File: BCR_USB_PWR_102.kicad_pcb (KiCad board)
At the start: 2 copper layers, 21.8 x 13.2 mm, 2 parts, among them CN1 DB9_Female, CN2 UE27AC54100

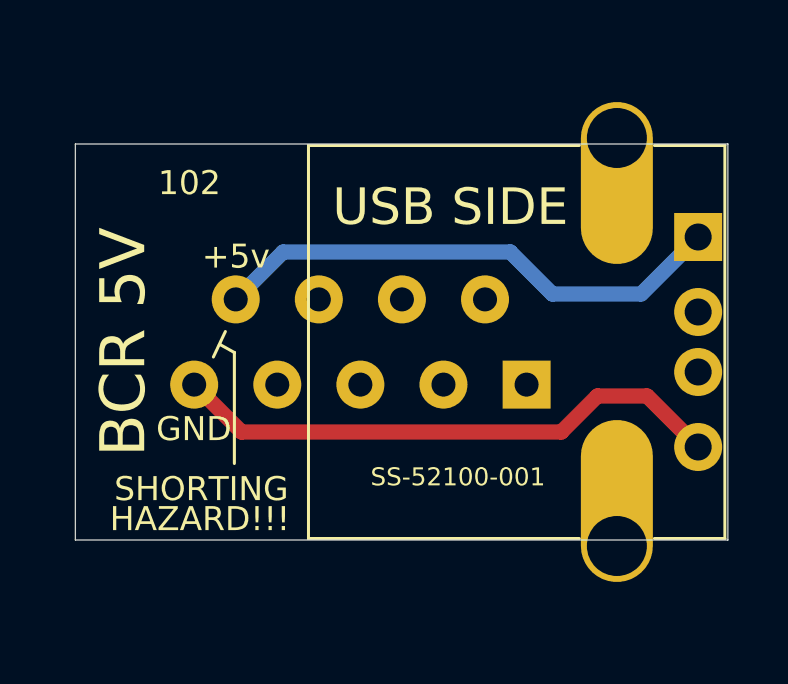
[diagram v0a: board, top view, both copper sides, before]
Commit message: rename NEC to up_long, and a short up version that covers up the shorting hazard
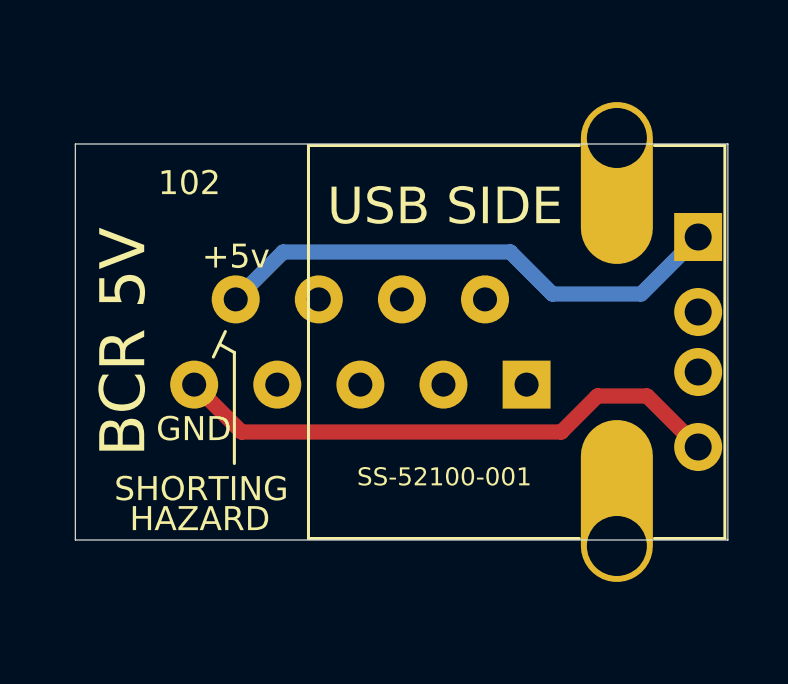
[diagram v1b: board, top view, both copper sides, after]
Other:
- board text added: "HAZARD"
- board text removed: "HAZARD!!!"
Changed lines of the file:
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@@
     (effects (font (size 0.8 0.8) (thickness 0.08)))
   )
-  (gr_text HAZARD!!! (at 121.65 101.658) (layer F.SilkS)
+  (gr_text HAZARD (at 121.65 101.658) (layer F.SilkS)
     (effects (font (size 0.8 0.8) (thickness 0.08)))
   )
@@
     (effects (font (size 0.6 0.6) (thickness 0.1)) (justify mirror))
   )
-  (gr_text SS-52100-001 (at 130.25 100.258) (layer F.SilkS)
+  (gr_text SS-52100-001 (at 129.8 100.258) (layer F.SilkS)
     (effects (font (size 0.6 0.6) (thickness 0.1)))
   )
@@
     (effects (font (size 1.2192 1.2192) (thickness 0.2032)) (justify mirror))
   )
-  (gr_text "USB SIDE" (at 130 91.258) (layer F.SilkS)
+  (gr_text "USB SIDE" (at 129.825 91.233) (layer F.SilkS)
     (effects (font (size 1.2192 1.2192) (thickness 0.2032)))
   )

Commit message: Add BCR_Breakout. Rename repo to BCR_Breakout.
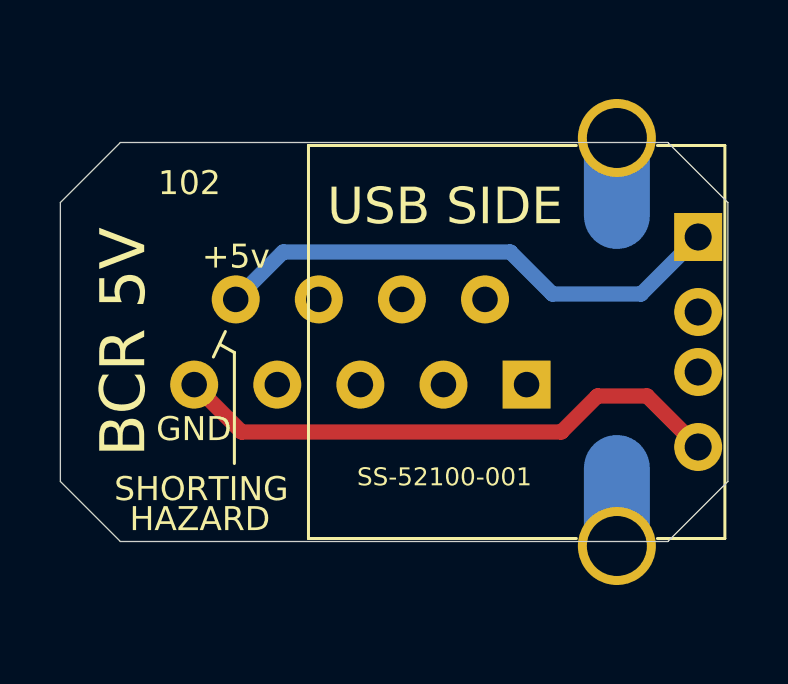
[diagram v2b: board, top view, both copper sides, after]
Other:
- board size 21.8 x 13.2 mm -> 22.2 x 13.3 mm
- board text added: "BCR to USB 5v"
- board text added: "github.com/bkw777/BCR_Breakout"
- board text removed: "5v USB power from BCR port"
- board text removed: "github.com/bkw777/BCR_USB_PWR"
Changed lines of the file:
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@@
   (general
     (thickness 1.6)
-    (drawings 26)
+    (drawings 30)
     (tracks 10)
     (zones 0)
@@
     (uvia_min_size 0.2)
     (uvia_min_drill 0.1)
-    (edge_width 0.05)
+    (edge_width 0.025)
     (segment_width 0.2)
     (pcb_text_width 0.3)
@@
     (add_net "Net-(CN2-PadSH)")
   )
-  (module 0_LOCAL:USB_A_Female_UE27AC54100_cut (layer F.Cu)
-    (at 135.55 95.758 270)
-    (fp_text reference CN2 (at 0 -0.889 270 unlocked) (layer F.SilkS) hide
-      (effects (font (size 1 1) (thickness 0.15)))
-    )
-    (fp_text value UE27AC54100 (at 0 11.35 270) (layer F.Fab)
-      (effects (font (size 1 1) (thickness 0.15)))
-    )
-    (fp_line (start -6.55 -3.6) (end 6.55 -3.6) (layer F.SilkS) (width 0.1))
-    (fp_line (start 6.55 1.25) (end 6.55 10.28) (layer F.SilkS) (width 0.1))
-    (fp_line (start -6.55 1.25) (end -6.55 10.28) (layer F.SilkS) (width 0.1))
-    (fp_line (start -6.55 -3.6) (end -6.55 -1.25) (layer F.SilkS) (width 0.1))
-    (fp_line (start -6.55 -3.6) (end 6.55 -3.6) (layer F.Fab) (width 0.1))
-    (fp_line (start 6.55 -3.6) (end 6.55 10.28) (layer F.Fab) (width 0.1))
-    (fp_line (start -6.55 -3.6) (end -6.55 10.28) (layer F.Fab) (width 0.1))
-    (fp_line (start -6.55 10.28) (end 6.55 10.28) (layer F.Fab) (width 0.1))
-    (fp_line (start 6.55 -3.6) (end 6.55 -1.25) (layer F.SilkS) (width 0.1))
-    (fp_line (start 6.55 10.28) (end -6.55 10.28) (layer F.SilkS) (width 0.1))
-    (fp_line (start -6.75 -3.94) (end 6.75 -3.94) (layer F.CrtYd) (width 0.05))
-    (fp_line (start 6.75 -3.94) (end 6.75 10.375) (layer F.CrtYd) (width 0.05))
-    (fp_line (start -6.75 -3.94) (end -6.75 10.375) (layer F.CrtYd) (width 0.05))
-    (fp_line (start -6.75 10.375) (end 6.75 10.375) (layer F.CrtYd) (width 0.05))
-    (fp_text user %R (at -0.025 0.975 270) (layer F.Fab)
-      (effects (font (size 1 1) (thickness 0.15)))
-    )
-    (pad 4 thru_hole circle (at 3.5 -2.71 270) (size 1.6 1.6) (drill 0.9) (layers *.Cu *.Mask)
-      (net 2 /GND))
-    (pad 3 thru_hole circle (at 1 -2.71 270) (size 1.6 1.6) (drill 0.9) (layers *.Cu *.Mask))
-    (pad 2 thru_hole circle (at -1 -2.71 270) (size 1.6 1.6) (drill 0.9) (layers *.Cu *.Mask))
-    (pad 1 thru_hole rect (at -3.5 -2.71 270) (size 1.6 1.6) (drill 0.9) (layers *.Cu *.Mask)
-      (net 1 /+5V))
-    (pad SH thru_hole oval (at 6.8 0 270) (size 5.4 2.4) (drill 2 (offset -1.5 0)) (layers *.Cu *.Mask)
-      (net 3 "Net-(CN2-PadSH)"))
-    (pad SH thru_hole oval (at -6.8 0 270) (size 5.4 2.4) (drill 2 (offset 1.5 0)) (layers *.Cu *.Mask)
-      (net 3 "Net-(CN2-PadSH)"))
-    (model ${KIPRJMOD}/3dmodels/USB-A_female_horiz_thru.step
-      (offset (xyz 0 3.5 6.9))
-      (scale (xyz 1 1 1))
-      (rotate (xyz 0 0 0))
-    )
-  )
   (module 0_LOCAL:DSUB-9_Female_Vertical_metal (layer B.Cu)
     (at 132.54 97.178)
@@
     (fp_line (start -5.54 -0.82) (end -5.54 -2.02) (layer Dwgs.User) (width 0.01))
     (fp_line (start -6.54 -1.42) (end -4.54 -1.42) (layer Dwgs.User) (width 0.01))
-    (pad 9 thru_hole circle (at -9.695 -2.84) (size 1.6 1.6) (drill 0.8) (layers *.Cu *.Mask)
+    (pad 9 thru_hole circle (at -9.695 -2.84) (size 1.6 1.6) (drill 0.85) (layers *.Cu *.Mask)
       (net 1 /+5V))
-    (pad 8 thru_hole circle (at -6.925 -2.84) (size 1.6 1.6) (drill 0.8) (layers *.Cu *.Mask))
-    (pad 7 thru_hole circle (at -4.155 -2.84) (size 1.6 1.6) (drill 0.8) (layers *.Cu *.Mask))
-    (pad 6 thru_hole circle (at -1.385 -2.84) (size 1.6 1.6) (drill 0.8) (layers *.Cu *.Mask))
-    (pad 5 thru_hole circle (at -11.08 0) (size 1.6 1.6) (drill 0.8) (layers *.Cu *.Mask)
+    (pad 8 thru_hole circle (at -6.925 -2.84) (size 1.6 1.6) (drill 0.85) (layers *.Cu *.Mask))
+    (pad 7 thru_hole circle (at -4.155 -2.84) (size 1.6 1.6) (drill 0.85) (layers *.Cu *.Mask))
+    (pad 6 thru_hole circle (at -1.385 -2.84) (size 1.6 1.6) (drill 0.85) (layers *.Cu *.Mask))
+    (pad 5 thru_hole circle (at -11.08 0) (size 1.6 1.6) (drill 0.85) (layers *.Cu *.Mask)
       (net 2 /GND))
-    (pad 4 thru_hole circle (at -8.31 0) (size 1.6 1.6) (drill 0.8) (layers *.Cu *.Mask))
-    (pad 3 thru_hole circle (at -5.54 0) (size 1.6 1.6) (drill 0.8) (layers *.Cu *.Mask))
-    (pad 2 thru_hole circle (at -2.77 0) (size 1.6 1.6) (drill 0.8) (layers *.Cu *.Mask))
-    (pad 1 thru_hole rect (at 0 0) (size 1.6 1.6) (drill 0.8) (layers *.Cu *.Mask))
+    (pad 4 thru_hole circle (at -8.31 0) (size 1.6 1.6) (drill 0.85) (layers *.Cu *.Mask))
+    (pad 3 thru_hole circle (at -5.54 0) (size 1.6 1.6) (drill 0.85) (layers *.Cu *.Mask))
+    (pad 2 thru_hole circle (at -2.77 0) (size 1.6 1.6) (drill 0.85) (layers *.Cu *.Mask))
+    (pad 1 thru_hole rect (at 0 0) (size 1.6 1.6) (drill 0.85) (layers *.Cu *.Mask))
     (model ${KIPRJMOD}/3dmodels/DE9F_metal.step
       (offset (xyz -5.528 -1.42 6.35))
@@
     )
   )
+  (module 0_LOCAL:USB_A_Female_UE27AC54100_cut (layer F.Cu)
+    (at 135.55 95.758 270)
+    (fp_text reference CN2 (at 0 -0.889 270 unlocked) (layer F.SilkS) hide
+      (effects (font (size 1 1) (thickness 0.15)))
+    )
+    (fp_text value UE27AC54100 (at 0 11.35 270) (layer F.Fab)
+      (effects (font (size 1 1) (thickness 0.15)))
+    )
+    (fp_line (start -6.55 -3.6) (end 6.55 -3.6) (layer F.SilkS) (width 0.1))
+    (fp_line (start 6.55 1.35) (end 6.55 10.28) (layer F.SilkS) (width 0.1))
+    (fp_line (start -6.55 1.35) (end -6.55 10.28) (layer F.SilkS) (width 0.1))
+    (fp_line (start -6.55 -3.6) (end -6.55 -1.35) (layer F.SilkS) (width 0.1))
+    (fp_line (start -6.55 -3.6) (end 6.55 -3.6) (layer F.Fab) (width 0.1))
+    (fp_line (start 6.55 -3.6) (end 6.55 10.28) (layer F.Fab) (width 0.1))
+    (fp_line (start -6.55 -3.6) (end -6.55 10.28) (layer F.Fab) (width 0.1))
+    (fp_line (start -6.55 10.28) (end 6.55 10.28) (layer F.Fab) (width 0.1))
+    (fp_line (start 6.55 -3.6) (end 6.55 -1.35) (layer F.SilkS) (width 0.1))
+    (fp_line (start 6.55 10.28) (end -6.55 10.28) (layer F.SilkS) (width 0.1))
+    (fp_line (start -6.75 -3.94) (end 6.75 -3.94) (layer F.CrtYd) (width 0.05))
+    (fp_line (start 6.75 -3.94) (end 6.75 10.375) (layer F.CrtYd) (width 0.05))
+    (fp_line (start -6.75 -3.94) (end -6.75 10.375) (layer F.CrtYd) (width 0.05))
+    (fp_line (start -6.75 10.375) (end 6.75 10.375) (layer F.CrtYd) (width 0.05))
+    (fp_text user %R (at -0.025 0.975 270) (layer F.Fab)
+      (effects (font (size 1 1) (thickness 0.15)))
+    )
+    (pad SH smd oval (at 7 0 270) (size 4.8 2.2) (drill (offset -1.5 0)) (layers B.Cu B.Paste B.Mask)
+      (net 3 "Net-(CN2-PadSH)"))
+    (pad SH smd oval (at -7 0 270) (size 4.8 2.2) (drill (offset 1.5 0)) (layers B.Cu B.Paste B.Mask)
+      (net 3 "Net-(CN2-PadSH)"))
+    (pad 4 thru_hole circle (at 3.5 -2.71 270) (size 1.6 1.6) (drill 0.9) (layers *.Cu *.Mask)
+      (net 2 /GND))
+    (pad 3 thru_hole circle (at 1 -2.71 270) (size 1.6 1.6) (drill 0.9) (layers *.Cu *.Mask))
+    (pad 2 thru_hole circle (at -1 -2.71 270) (size 1.6 1.6) (drill 0.9) (layers *.Cu *.Mask))
+    (pad 1 thru_hole rect (at -3.5 -2.71 270) (size 1.6 1.6) (drill 0.9) (layers *.Cu *.Mask)
+      (net 1 /+5V))
+    (pad SH thru_hole circle (at 6.8 0 270) (size 2.6 2.6) (drill 2) (layers *.Cu *.Mask)
+      (net 3 "Net-(CN2-PadSH)"))
+    (pad SH thru_hole circle (at -6.8 0 270) (size 2.6 2.6) (drill 2) (layers *.Cu *.Mask)
+      (net 3 "Net-(CN2-PadSH)"))
+    (model ${KIPRJMOD}/3dmodels/USB-A_female_horiz_thru.step
+      (offset (xyz 0 3.5 6.9))
+      (scale (xyz 1 1 1))
+      (rotate (xyz 0 0 0))
+    )
+  )
+  (gr_line (start 117 100.408) (end 117 91.108) (layer Edge.Cuts) (width 0.025))
+  (gr_line (start 137.25 89.108) (end 119 89.108) (layer Edge.Cuts) (width 0.025))
+  (gr_line (start 139.25 100.408) (end 139.25 91.108) (layer Edge.Cuts) (width 0.025))
+  (gr_line (start 137.25 102.408) (end 119 102.408) (layer Edge.Cuts) (width 0.025))
+  (gr_line (start 119 89.108) (end 117 91.108) (layer Edge.Cuts) (width 0.025))
+  (gr_line (start 139.25 91.108) (end 137.25 89.108) (layer Edge.Cuts) (width 0.025))
+  (gr_line (start 137.25 102.408) (end 139.25 100.408) (layer Edge.Cuts) (width 0.025))
+  (gr_line (start 117 100.408) (end 119 102.408) (layer Edge.Cuts) (width 0.025))
   (gr_line (start 122.1 96.258) (end 122.5 95.408) (layer F.SilkS) (width 0.1016))
   (gr_line (start 122.8 96.108) (end 122.35 95.858) (layer F.SilkS) (width 0.1016))
@@
     (effects (font (size 0.6 0.6) (thickness 0.1)))
   )
-  (gr_text github.com/bkw777/BCR_USB_PWR (at 125.9 101.458) (layer B.SilkS)
+  (gr_text github.com/bkw777/BCR_Breakout (at 126.45 101.408) (layer B.SilkS)
     (effects (font (size 0.6 0.6) (thickness 0.1)) (justify mirror))
   )
@@
     (effects (font (size 0.6 0.6) (thickness 0.1)) (justify mirror))
   )
-  (gr_text "5v USB power from BCR port" (at 125.8 89.858) (layer B.SilkS)
-    (effects (font (size 0.9 0.7) (thickness 0.1)) (justify mirror))
+  (gr_text "BCR to USB 5v" (at 125.8 89.858) (layer B.SilkS)
+    (effects (font (size 1 1) (thickness 0.15)) (justify mirror))
   )
   (gr_line (start 114.3 87.376) (end 139.7 104.14) (layer Dwgs.User) (width 0.0254))
@@
     (effects (font (size 1.2192 1.2192) (thickness 0.2032)))
   )
-  (gr_line (start 117.5 89.158) (end 117.5 102.358) (layer Edge.Cuts) (width 0.0254))
-  (gr_line (start 139.25 89.158) (end 117.5 89.158) (layer Edge.Cuts) (width 0.0254))
-  (gr_line (start 139.25 102.358) (end 139.25 89.158) (layer Edge.Cuts) (width 0.0254))
-  (gr_line (start 117.5 102.358) (end 139.25 102.358) (layer Edge.Cuts) (width 0.0254))
   (segment (start 133.4 94.158) (end 132 92.758) (width 0.508) (layer B.Cu) (net 1))
   (segment (start 132 92.758) (end 124.425 92.758) (width 0.508) (layer B.Cu) (net 1))

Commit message: change metal db9 to plastic
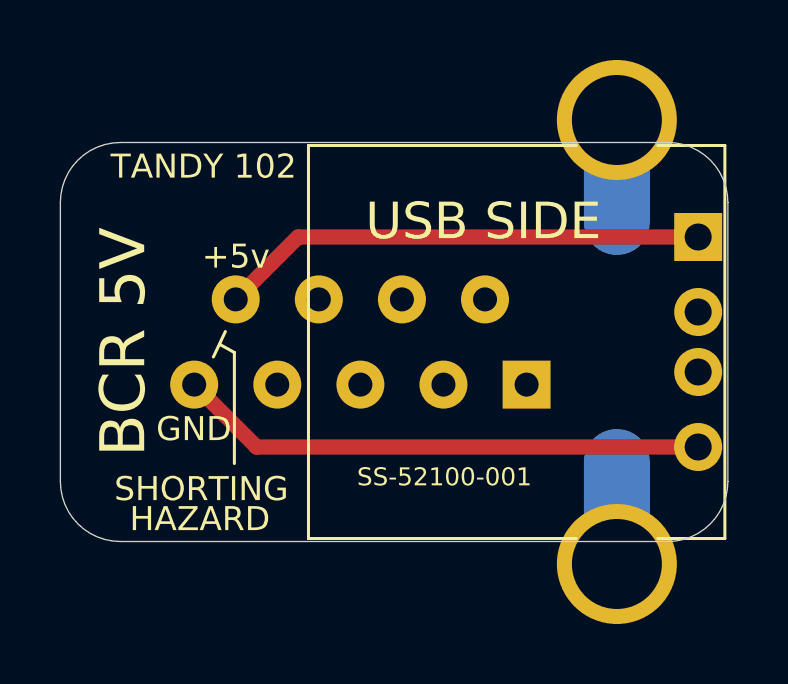
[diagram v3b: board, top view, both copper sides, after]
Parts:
- CN1: footprint 0_LOCAL:DSUB-9_Female_Vertical_metal -> 0_LOCAL:TE-5207826_cut
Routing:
- net /+5V: track 17.4 -> 16.3 mm
- net /GND: track 18.7 -> 17.7 mm
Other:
- board text added: "TE 5207826"
- board text removed: "102"
- board text removed: "A-DF 09 PP/Z"
